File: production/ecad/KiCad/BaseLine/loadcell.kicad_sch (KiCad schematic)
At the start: 19 parts, among them J4 LoadCellConnector, J9 ConnToESP32, U11 TXB0104DR, U6 MIC920YC5-TR, U7 MIC920YC5-TR, U8 ADS1231IDR

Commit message: footprint stuff
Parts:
- J9: footprint BLT:JST_B2B-XH-A -> (none)
- R55: value R_US -> DNP
- TP20, TP25: footprint TestPoint:TestPoint_2Pads_Pitch2.54mm_Drill0.8mm -> (none)
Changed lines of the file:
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@@
 			)
 		)
-		(property "Footprint" "TestPoint:TestPoint_2Pads_Pitch2.54mm_Drill0.8mm"
+		(property "Footprint" ""
 			(at 38.1 119.38 0)
 			(effects
@@
 			)
 		)
-		(property "Footprint" "BLT:JST_B2B-XH-A"
+		(property "Footprint" ""
 			(at 264.16 93.98 0)
 			(effects
@@
 			)
 		)
-		(property "Footprint" "TestPoint:TestPoint_2Pads_Pitch2.54mm_Drill0.8mm"
+		(property "Footprint" ""
 			(at 38.1 125.73 0)
 			(effects
@@
 			)
 		)
-		(property "Value" "R_US"
+		(property "Value" "DNP"
 			(at 67.31 196.596 90)
 			(effects

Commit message: Connectors and heirarchal labels
added connectors for power on the Loadcell schem and the battery schem

added the MCU heirarchal labels
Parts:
- added J15: Conn_to_Power, symbol Connector:Conn_01x02_Socket
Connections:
- net +5V: now also J15.1 (Pin_1)
- net GND: now also J15.2 (Pin_2)
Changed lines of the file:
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@@
 	(wire
 		(pts
+			(xy 168.91 24.13) (xy 172.72 24.13)
+		)
+		(stroke
+			(width 0)
+			(type default)
+		)
+	)
+	(wire
+		(pts
 			(xy 63.5 194.31) (xy 31.75 194.31)
 		)
@@
 	(wire
 		(pts
+			(xy 168.91 21.59) (xy 172.72 21.59)
+		)
+		(stroke
+			(width 0)
+			(type default)
+		)
+	)
+	(wire
+		(pts
 			(xy 124.46 104.14) (xy 124.46 101.6)
 		)
@@
 	)
 	(symbol
+		(lib_id "Connector:Conn_01x02_Socket")
+		(at 177.8 21.59 0)
+		(unit 1)
+		(exclude_from_sim no)
+		(in_bom yes)
+		(on_board yes)
+		(dnp no)
+		(fields_autoplaced yes)
+		(property "Reference" "J15"
+			(at 179.07 21.5899 0)
+			(effects
+				(font
+					(size 1.27 1.27)
+				)
+				(justify left)
+			)
+		)
+		(property "Value" "Conn_to_Power"
+			(at 179.07 24.1299 0)
+			(effects
+				(font
+					(size 1.27 1.27)
+				)
+				(justify left)
+			)
+		)
+		(property "Footprint" ""
+			(at 177.8 21.59 0)
+			(effects
+				(font
+					(size 1.27 1.27)
+				)
+				(hide yes)
+			)
+		)
+		(property "Datasheet" "~"
+			(at 177.8 21.59 0)
+			(effects
+				(font
+					(size 1.27 1.27)
+				)
+				(hide yes)
+			)
+		)
+		(property "Description" "Generic connector, single row, 01x02, script generated"
+			(at 177.8 21.59 0)
+			(effects
+				(font
+					(size 1.27 1.27)
+				)
+				(hide yes)
+			)
+		)
+		(pin "2"
+		)
+		(pin "1"
+		)
+		(instances
+			(project ""
+				(path "/ba9eda21-3882-41e1-8265-3d8ac781da20/15451660-bad9-4e79-85d3-2d59df8c5ccd"
+					(reference "J15")
+					(unit 1)
+				)
+			)
+		)
+	)
+	(symbol
 		(lib_id "Connector:Conn_01x04_Socket")
 		(at 36.83 87.63 0)
@@
 	)
 	(symbol
+		(lib_id "power:+5V")
+		(at 168.91 21.59 0)
+		(unit 1)
+		(exclude_from_sim no)
+		(in_bom yes)
+		(on_board yes)
+		(dnp no)
+		(property "Reference" "#PWR0116"
+			(at 168.91 25.4 0)
+			(effects
+				(font
+					(size 1.27 1.27)
+				)
+				(hide yes)
+			)
+		)
+		(property "Value" "+5V"
+			(at 168.91 16.51 0)
+			(effects
+				(font
+					(size 1.27 1.27)
+				)
+			)
+		)
+		(property "Footprint" ""
+			(at 168.91 21.59 0)
+			(effects
+				(font
+					(size 1.27 1.27)
+				)
+				(hide yes)
+			)
+		)
+		(property "Datasheet" ""
+			(at 168.91 21.59 0)
+			(effects
+				(font
+					(size 1.27 1.27)
+				)
+				(hide yes)
+			)
+		)
+		(property "Description" "Power symbol creates a global label with name \"+5V\""
+			(at 168.91 21.59 0)
+			(effects
+				(font
+					(size 1.27 1.27)
+				)
+				(hide yes)
+			)
+		)
+		(pin "1"
+		)
+		(instances
+			(project "BaseLine"
+				(path "/ba9eda21-3882-41e1-8265-3d8ac781da20/15451660-bad9-4e79-85d3-2d59df8c5ccd"
+					(reference "#PWR0116")
+					(unit 1)
+				)
+			)
+		)
+	)
+	(symbol
 		(lib_name "MIC920YC5-TR_1")
 		(lib_id "2024-10-08_01-43-59:MIC920YC5-TR")
@@
 					(unit 1)
 				)
+			)
+		)
+	)
+	(symbol
+		(lib_id "power:GND")
+		(at 168.91 24.13 0)
+		(unit 1)
+		(exclude_from_sim no)
+		(in_bom yes)
+		(on_board yes)
+		(dnp no)
+		(property "Reference" "#PWR0117"
+			(at 168.91 30.48 0)
+			(effects
+				(font
+					(size 1.27 1.27)
+				)
+				(hide yes)
+			)
+		)
+		(property "Value" "GND"
+			(at 169.164 28.194 0)
+			(effects
+				(font
+					(size 1.27 1.27)
+				)
+			)
+		)
+		(property "Footprint" ""
+			(at 168.91 24.13 0)
+			(effects
+				(font
+					(size 1.27 1.27)
+				)
+				(hide yes)
+			)
+		)
+		(property "Datasheet" ""
+			(at 168.91 24.13 0)
+			(effects
+				(font
+					(size 1.27 1.27)
+				)
+				(hide yes)
+			)
+		)
+		(property "Description" "Power symbol creates a global label with name \"GND\" , ground"
+			(at 168.91 24.13 0)
+			(effects
+				(font
+					(size 1.27 1.27)
+				)
+				(hide yes)
+			)
+		)
+		(pin "1"
+		)
+		(instances
+			(project "BaseLine"
+				(path "/ba9eda21-3882-41e1-8265-3d8ac781da20/15451660-bad9-4e79-85d3-2d59df8c5ccd"
+					(reference "#PWR0117")
+					(unit 1)
+				)

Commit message: fixing connectors I placed
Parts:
- removed J15: Conn_to_Power, symbol Connector:Conn_01x02_Socket
- added J15: power_for_Loadcell, symbol Connector:Conn_01x03_Socket
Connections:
- net +3.3V: now also J15.1 (Pin_1)
- net +5V: now also J15.2 (Pin_2)
- net GND: now also J15.3 (Pin_3)
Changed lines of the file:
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@@
 	(wire
 		(pts
+			(xy 171.45 25.4) (xy 173.99 25.4)
+		)
+		(stroke
+			(width 0)
+			(type default)
+		)
+	)
+	(wire
+		(pts
 			(xy 91.44 88.9) (xy 124.46 88.9)
 		)
@@
 	(wire
 		(pts
-			(xy 168.91 24.13) (xy 172.72 24.13)
+			(xy 170.18 30.48) (xy 173.99 30.48)
 		)
 		(stroke
@@
 	(wire
 		(pts
-			(xy 168.91 21.59) (xy 172.72 21.59)
+			(xy 166.37 27.94) (xy 173.99 27.94)
 		)
 		(stroke
@@
 	)
 	(symbol
-		(lib_id "Connector:Conn_01x02_Socket")
-		(at 177.8 21.59 0)
-		(unit 1)
-		(exclude_from_sim no)
-		(in_bom yes)
-		(on_board yes)
-		(dnp no)
-		(fields_autoplaced yes)
-		(property "Reference" "J15"
-			(at 179.07 21.5899 0)
-			(effects
-				(font
-					(size 1.27 1.27)
-				)
-				(justify left)
-			)
-		)
-		(property "Value" "Conn_to_Power"
-			(at 179.07 24.1299 0)
-			(effects
-				(font
-					(size 1.27 1.27)
-				)
-				(justify left)
-			)
-		)
-		(property "Footprint" ""
-			(at 177.8 21.59 0)
-			(effects
-				(font
-					(size 1.27 1.27)
-				)
-				(hide yes)
-			)
-		)
-		(property "Datasheet" "~"
-			(at 177.8 21.59 0)
-			(effects
-				(font
-					(size 1.27 1.27)
-				)
-				(hide yes)
-			)
-		)
-		(property "Description" "Generic connector, single row, 01x02, script generated"
-			(at 177.8 21.59 0)
-			(effects
-				(font
-					(size 1.27 1.27)
-				)
-				(hide yes)
-			)
-		)
-		(pin "2"
-		)
-		(pin "1"
-		)
-		(instances
-			(project ""
-				(path "/ba9eda21-3882-41e1-8265-3d8ac781da20/15451660-bad9-4e79-85d3-2d59df8c5ccd"
-					(reference "J15")
-					(unit 1)
-				)
-			)
-		)
-	)
-	(symbol
 		(lib_id "Connector:Conn_01x04_Socket")
 		(at 36.83 87.63 0)
@@
 	)
 	(symbol
+		(lib_id "power:+3.3V")
+		(at 171.45 25.4 0)
+		(unit 1)
+		(exclude_from_sim no)
+		(in_bom yes)
+		(on_board yes)
+		(dnp no)
+		(fields_autoplaced yes)
+		(property "Reference" "#PWR0120"
+			(at 171.45 29.21 0)
+			(effects
+				(font
+					(size 1.27 1.27)
+				)
+				(hide yes)
+			)
+		)
+		(property "Value" "+3.3V"
+			(at 171.45 20.32 0)
+			(effects
+				(font
+					(size 1.27 1.27)
+				)
+			)
+		)
+		(property "Footprint" ""
+			(at 171.45 25.4 0)
+			(effects
+				(font
+					(size 1.27 1.27)
+				)
+				(hide yes)
+			)
+		)
+		(property "Datasheet" ""
+			(at 171.45 25.4 0)
+			(effects
+				(font
+					(size 1.27 1.27)
+				)
+				(hide yes)
+			)
+		)
+		(property "Description" "Power symbol creates a global label with name \"+3.3V\""
+			(at 171.45 25.4 0)
+			(effects
+				(font
+					(size 1.27 1.27)
+				)
+				(hide yes)
+			)
+		)
+		(pin "1"
+		)
+		(instances
+			(project ""
+				(path "/ba9eda21-3882-41e1-8265-3d8ac781da20/15451660-bad9-4e79-85d3-2d59df8c5ccd"
+					(reference "#PWR0120")
+					(unit 1)
+				)
+			)
+		)
+	)
+	(symbol
 		(lib_id "Device:R_US")
 		(at 36.83 142.24 270)
@@
 	(symbol
 		(lib_id "power:+5V")
-		(at 168.91 21.59 0)
+		(at 166.37 27.94 0)
 		(unit 1)
 		(exclude_from_sim no)
@@
 		(dnp no)
 		(property "Reference" "#PWR0116"
-			(at 168.91 25.4 0)
+			(at 166.37 31.75 0)
 			(effects
 				(font
@@
 		)
 		(property "Value" "+5V"
-			(at 168.91 16.51 0)
+			(at 166.37 22.86 0)
 			(effects
 				(font
@@
 		)
 		(property "Footprint" ""
-			(at 168.91 21.59 0)
+			(at 166.37 27.94 0)
 			(effects
 				(font
@@
 		)
 		(property "Datasheet" ""
-			(at 168.91 21.59 0)
+			(at 166.37 27.94 0)
 			(effects
 				(font
@@
 		)
 		(property "Description" "Power symbol creates a global label with name \"+5V\""
-			(at 168.91 21.59 0)
+			(at 166.37 27.94 0)
 			(effects
 				(font
@@
 	)
 	(symbol
+		(lib_id "Connector:Conn_01x03_Socket")
+		(at 179.07 27.94 0)
+		(unit 1)
+		(exclude_from_sim no)
+		(in_bom yes)
+		(on_board yes)
+		(dnp no)
+		(fields_autoplaced yes)
+		(property "Reference" "J15"
+			(at 180.34 26.6699 0)
+			(effects
+				(font
+					(size 1.27 1.27)
+				)
+				(justify left)
+			)
+		)
+		(property "Value" "power_for_Loadcell"
+			(at 180.34 29.2099 0)
+			(effects
+				(font
+					(size 1.27 1.27)
+				)
+				(justify left)
+			)
+		)
+		(property "Footprint" ""
+			(at 179.07 27.94 0)
+			(effects
+				(font
+					(size 1.27 1.27)
+				)
+				(hide yes)
+			)
+		)
+		(property "Datasheet" "~"
+			(at 179.07 27.94 0)
+			(effects
+				(font
+					(size 1.27 1.27)
+				)
+				(hide yes)
+			)
+		)
+		(property "Description" "Generic connector, single row, 01x03, script generated"
+			(at 179.07 27.94 0)
+			(effects
+				(font
+					(size 1.27 1.27)
+				)
+				(hide yes)
+			)
+		)
+		(pin "2"
+		)
+		(pin "3"
+		)
+		(pin "1"
+		)
+		(instances
+			(project ""
+				(path "/ba9eda21-3882-41e1-8265-3d8ac781da20/15451660-bad9-4e79-85d3-2d59df8c5ccd"
+					(reference "J15")
+					(unit 1)
+				)
+			)
+		)
+	)
+	(symbol
 		(lib_id "power:GND")
 		(at 190.5 78.74 0)
@@
 	(symbol
 		(lib_id "power:GND")
-		(at 168.91 24.13 0)
+		(at 170.18 30.48 0)
 		(unit 1)
 		(exclude_from_sim no)
@@
 		(dnp no)
 		(property "Reference" "#PWR0117"
-			(at 168.91 30.48 0)
+			(at 170.18 36.83 0)
 			(effects
 				(font
@@
 		)
 		(property "Value" "GND"
-			(at 169.164 28.194 0)
+			(at 170.434 34.544 0)
 			(effects
 				(font
@@
 		)
 		(property "Footprint" ""
-			(at 168.91 24.13 0)
+			(at 170.18 30.48 0)
 			(effects
 				(font
@@
 		)
 		(property "Datasheet" ""
-			(at 168.91 24.13 0)
+			(at 170.18 30.48 0)
 			(effects
 				(font
@@
 		)
 		(property "Description" "Power symbol creates a global label with name \"GND\" , ground"
-			(at 168.91 24.13 0)
+			(at 170.18 30.48 0)
 			(effects
 				(font

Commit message: fixed Faultn pull up to 3.3V
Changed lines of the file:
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@@
 		(on_board yes)
 		(dnp no)
-		(fields_autoplaced yes)
 		(property "Reference" "#PWR061"
 			(at 190.5 85.09 0)
@@
 		)
 		(property "Value" "GND"
-			(at 190.5 83.82 0)
+			(at 194.818 80.518 0)
 			(effects
 				(font

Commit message: Updated footprints
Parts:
- C: renamed from VAR1; value C -> VAR
- J15: footprint (none) -> Connector_JST:JST_EH_B3B-EH-A_1x03_P2.50mm_Vertical
- J4: footprint BLT:JST_B2B-XH-A -> Connector_JST:JST_EH_B4B-EH-A_1x04_P2.50mm_Vertical; ConnLink (none) -> https://www.digikey.com/en/products/detail/jst-sales-americ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
- J9: footprint (none) -> Connector_JST:JST_EH_B4B-EH-A_1x04_P2.50mm_Vertical
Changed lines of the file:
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@@
 			)
 		)
-		(property "Footprint" "BLT:JST_B2B-XH-A"
+		(property "Footprint" "Connector_JST:JST_EH_B4B-EH-A_1x04_P2.50mm_Vertical"
 			(at 36.83 87.63 0)
 			(effects
@@
 		)
 		(property "Description" " FX1901-0001-0200-L"
+			(at 36.83 87.63 0)
+			(effects
+				(font
+					(size 1.27 1.27)
+				)
+				(hide yes)
+			)
+		)
+		(property "ConnLink" "https://www.digikey.com/en/products/detail/jst-sales-america-inc/B4B-EH-A/758748?s=N4IgTCBcDaIEIBY4FoCiAJZBBEBdAvkA"
 			(at 36.83 87.63 0)
 			(effects
@@
 			)
 		)
-		(property "Footprint" ""
+		(property "Footprint" "Connector_JST:JST_EH_B4B-EH-A_1x04_P2.50mm_Vertical"
 			(at 264.16 93.98 0)
 			(effects
@@
 			)
 		)
-		(property "Datasheet" "~"
+		(property "Datasheet" "https://www.digikey.com/en/products/detail/jst-sales-america-inc/B4B-EH-A/758748?s=N4IgTCBcDaIEIBY4FoCiAJZBBEBdAvkA"
 			(at 264.16 93.98 0)
 			(effects
@@
 		)
 		(instances
-			(project ""
+			(project "BaseLine"
 				(path "/ba9eda21-3882-41e1-8265-3d8ac781da20/15451660-bad9-4e79-85d3-2d59df8c5ccd"
 					(reference "#PWR0120")
@@
 		(on_board yes)
 		(dnp no)
-		(fields_autoplaced yes)
 		(property "Reference" "C18"
-			(at 46.99 144.7799 0)
+			(at 44.704 144.018 0)
 			(effects
 				(font
@@
 		)
 		(property "Value" "VAR"
-			(at 46.99 147.3199 0)
+			(at 44.45 148.336 0)
 			(effects
 				(font
@@
 			)
 		)
-		(property "Footprint" ""
+		(property "Footprint" "Connector_JST:JST_EH_B3B-EH-A_1x03_P2.50mm_Vertical"
 			(at 179.07 27.94 0)
 			(effects
@@
 		)
 		(instances
-			(project ""
+			(project "BaseLine"
 				(path "/ba9eda21-3882-41e1-8265-3d8ac781da20/15451660-bad9-4e79-85d3-2d59df8c5ccd"
 					(reference "J15")
@@
 		(on_board yes)
 		(dnp no)
-		(property "Reference" "VAR1"
-			(at 46.482 182.626 0)
-			(effects
-				(font
-					(size 1.27 1.27)
-				)
-			)
-		)
-		(property "Value" "C"
-			(at 46.228 180.594 0)
+		(property "Reference" "C"
+			(at 45.974 183.896 0)
+			(effects
+				(font
+					(size 1.27 1.27)
+				)
+			)
+		)
+		(property "Value" "VAR"
+			(at 44.704 179.324 0)
 			(effects
 				(font
@@
 			(project "BaseLine"
 				(path "/ba9eda21-3882-41e1-8265-3d8ac781da20/15451660-bad9-4e79-85d3-2d59df8c5ccd"
-					(reference "VAR1")
-					(unit 1)
-				)
+					(reference "C")
+					(unit 1)
+				)

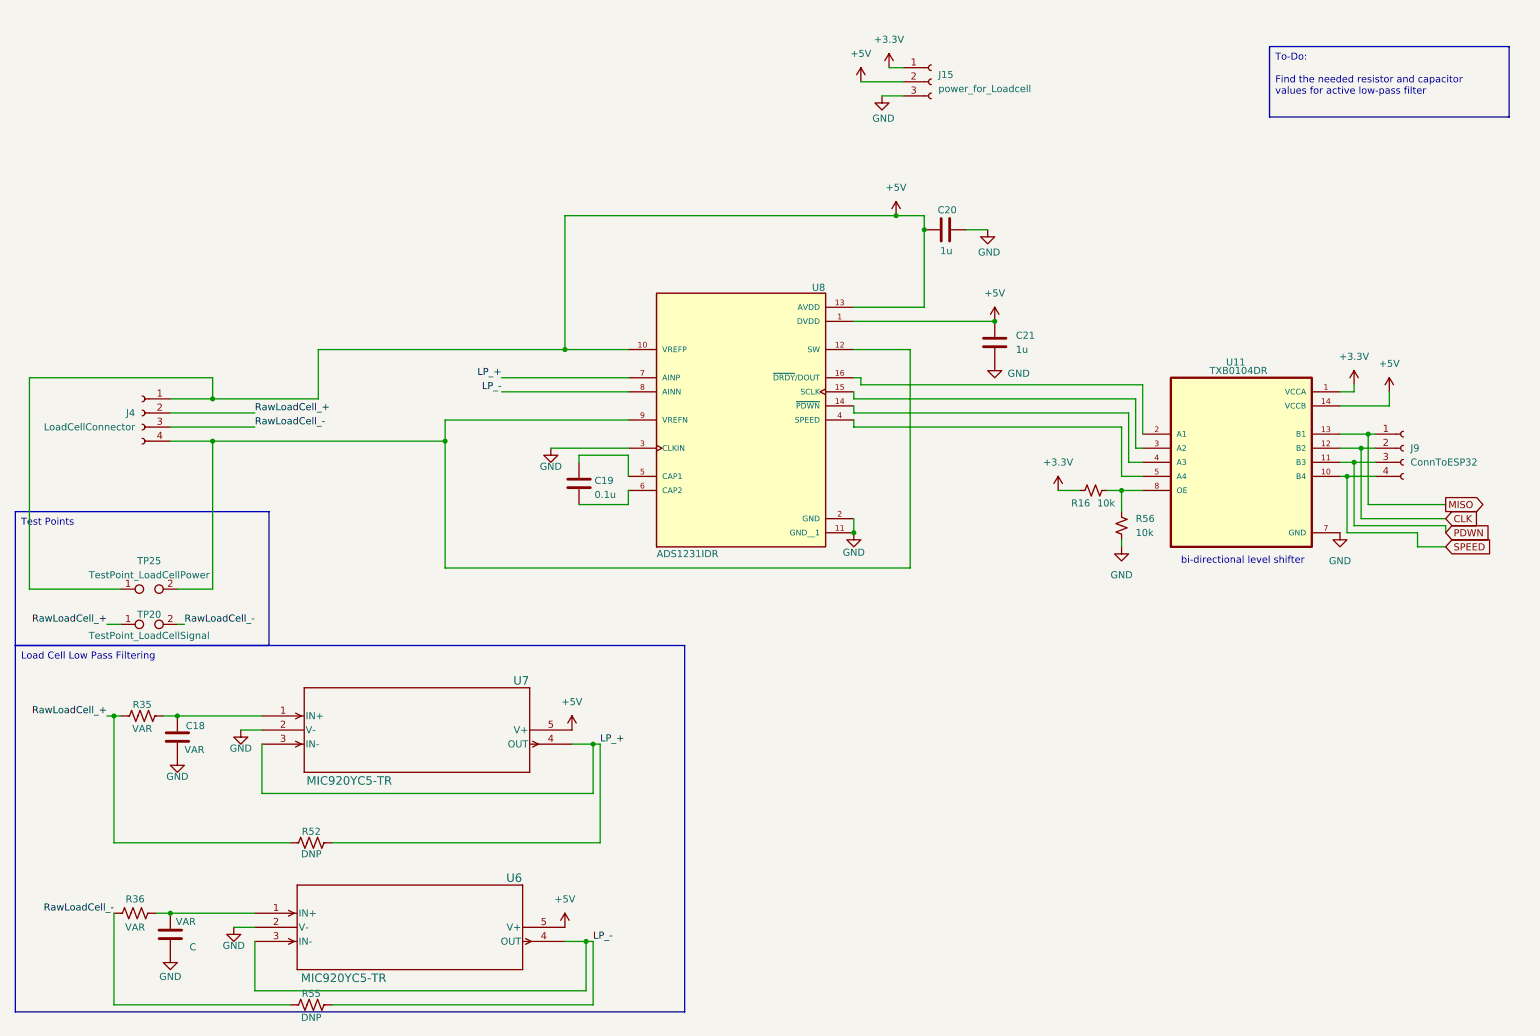
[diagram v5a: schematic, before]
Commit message: fixed level shifters
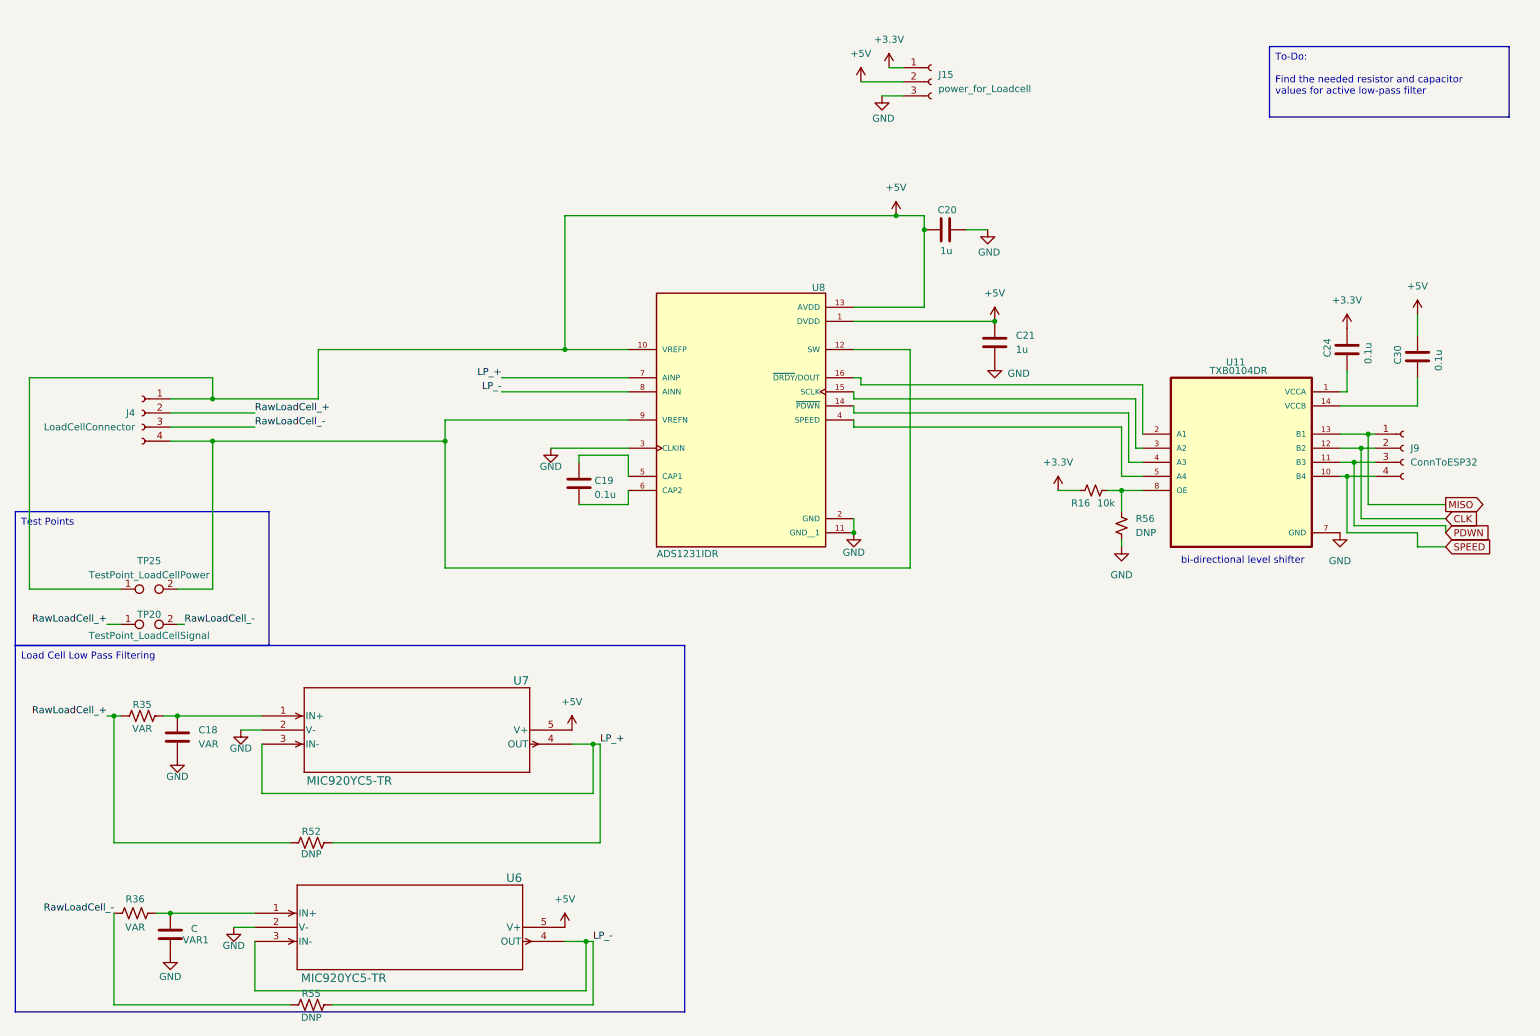
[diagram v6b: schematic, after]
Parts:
- added C24, C30: 0.1u, Capacitor_SMD:C_0805_2012Metric_Pad1.18x1.45mm_HandSolder, symbol Device:C
- J15: footprint Connector_JST:JST_EH_B3B-EH-A_1x03_P2.50mm_Vertical -> (none)
- J4: footprint Connector_JST:JST_EH_B4B-EH-A_1x04_P2.50mm_Vertical -> BLT:JST_B2B-XH-A; ConnLink https://www.digikey.com/en/products/detail/jst-sales-americ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 -> (none)
- J9: footprint Connector_JST:JST_EH_B4B-EH-A_1x04_P2.50mm_Vertical -> (none)
- R56: value 10k -> DNP
- VAR1: renamed from C; value VAR -> C
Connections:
- net +3.3V: now also C24.2; no longer U11.1 (VCCA)
- net +5V: now also C30.2; no longer U11.14 (VCCB)
- new net: C24.1, U11.1 (VCCA)
- new net: C30.1, U11.14 (VCCB)

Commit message: Updated load cell footprints
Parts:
- J15: footprint (none) -> Connector_JST:JST_EH_B3B-EH-A_1x03_P2.50mm_Vertical
- J4: footprint BLT:JST_B2B-XH-A -> Connector_JST:JST_EH_B4B-EH-A_1x04_P2.50mm_Vertical
- J9: footprint (none) -> Connector_JST:JST_EH_B4B-EH-A_1x04_P2.50mm_Vertical
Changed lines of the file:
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@@
 			)
 		)
-		(property "Footprint" "BLT:JST_B2B-XH-A"
+		(property "Footprint" "Connector_JST:JST_EH_B4B-EH-A_1x04_P2.50mm_Vertical"
 			(at 36.83 87.63 0)
 			(effects
@@
 			)
 		)
-		(property "Footprint" ""
+		(property "Footprint" "Connector_JST:JST_EH_B4B-EH-A_1x04_P2.50mm_Vertical"
 			(at 264.16 93.98 0)
 			(effects
@@
 		)
 		(instances
-			(project ""
+			(project "BaseLine"
 				(path "/ba9eda21-3882-41e1-8265-3d8ac781da20/15451660-bad9-4e79-85d3-2d59df8c5ccd"
 					(reference "#PWR0120")
@@
 			)
 		)
-		(property "Footprint" ""
+		(property "Footprint" "Connector_JST:JST_EH_B3B-EH-A_1x03_P2.50mm_Vertical"
 			(at 179.07 27.94 0)
 			(effects
@@
 		)
 		(instances
-			(project ""
+			(project "BaseLine"
 				(path "/ba9eda21-3882-41e1-8265-3d8ac781da20/15451660-bad9-4e79-85d3-2d59df8c5ccd"
 					(reference "J15")

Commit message: added imu pretty folder and some footprints battery
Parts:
- J15: footprint Connector_JST:JST_EH_B3B-EH-A_1x03_P2.50mm_Vertical -> (none)
- J4: footprint Connector_JST:JST_EH_B4B-EH-A_1x04_P2.50mm_Vertical -> BLT:JST_B2B-XH-A
- J9: footprint Connector_JST:JST_EH_B4B-EH-A_1x04_P2.50mm_Vertical -> (none)
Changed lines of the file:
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@@
 			)
 		)
-		(property "Footprint" "Connector_JST:JST_EH_B4B-EH-A_1x04_P2.50mm_Vertical"
+		(property "Footprint" "BLT:JST_B2B-XH-A"
 			(at 36.83 87.63 0)
 			(effects
@@
 			)
 		)
-		(property "Footprint" "Connector_JST:JST_EH_B4B-EH-A_1x04_P2.50mm_Vertical"
+		(property "Footprint" ""
 			(at 264.16 93.98 0)
 			(effects
@@
 		)
 		(instances
-			(project "BaseLine"
+			(project ""
 				(path "/ba9eda21-3882-41e1-8265-3d8ac781da20/15451660-bad9-4e79-85d3-2d59df8c5ccd"
 					(reference "#PWR0120")
@@
 			)
 		)
-		(property "Footprint" "Connector_JST:JST_EH_B3B-EH-A_1x03_P2.50mm_Vertical"
+		(property "Footprint" ""
 			(at 179.07 27.94 0)
 			(effects
@@
 		)
 		(instances
-			(project "BaseLine"
+			(project ""
 				(path "/ba9eda21-3882-41e1-8265-3d8ac781da20/15451660-bad9-4e79-85d3-2d59df8c5ccd"
 					(reference "J15")
